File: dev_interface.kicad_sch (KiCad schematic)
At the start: 18 parts, among them U10 ADS1014IDGS, U11 DACx53401, U12 ADS1014IDGS, U4 TLV9302xD, U9 ISO164xB

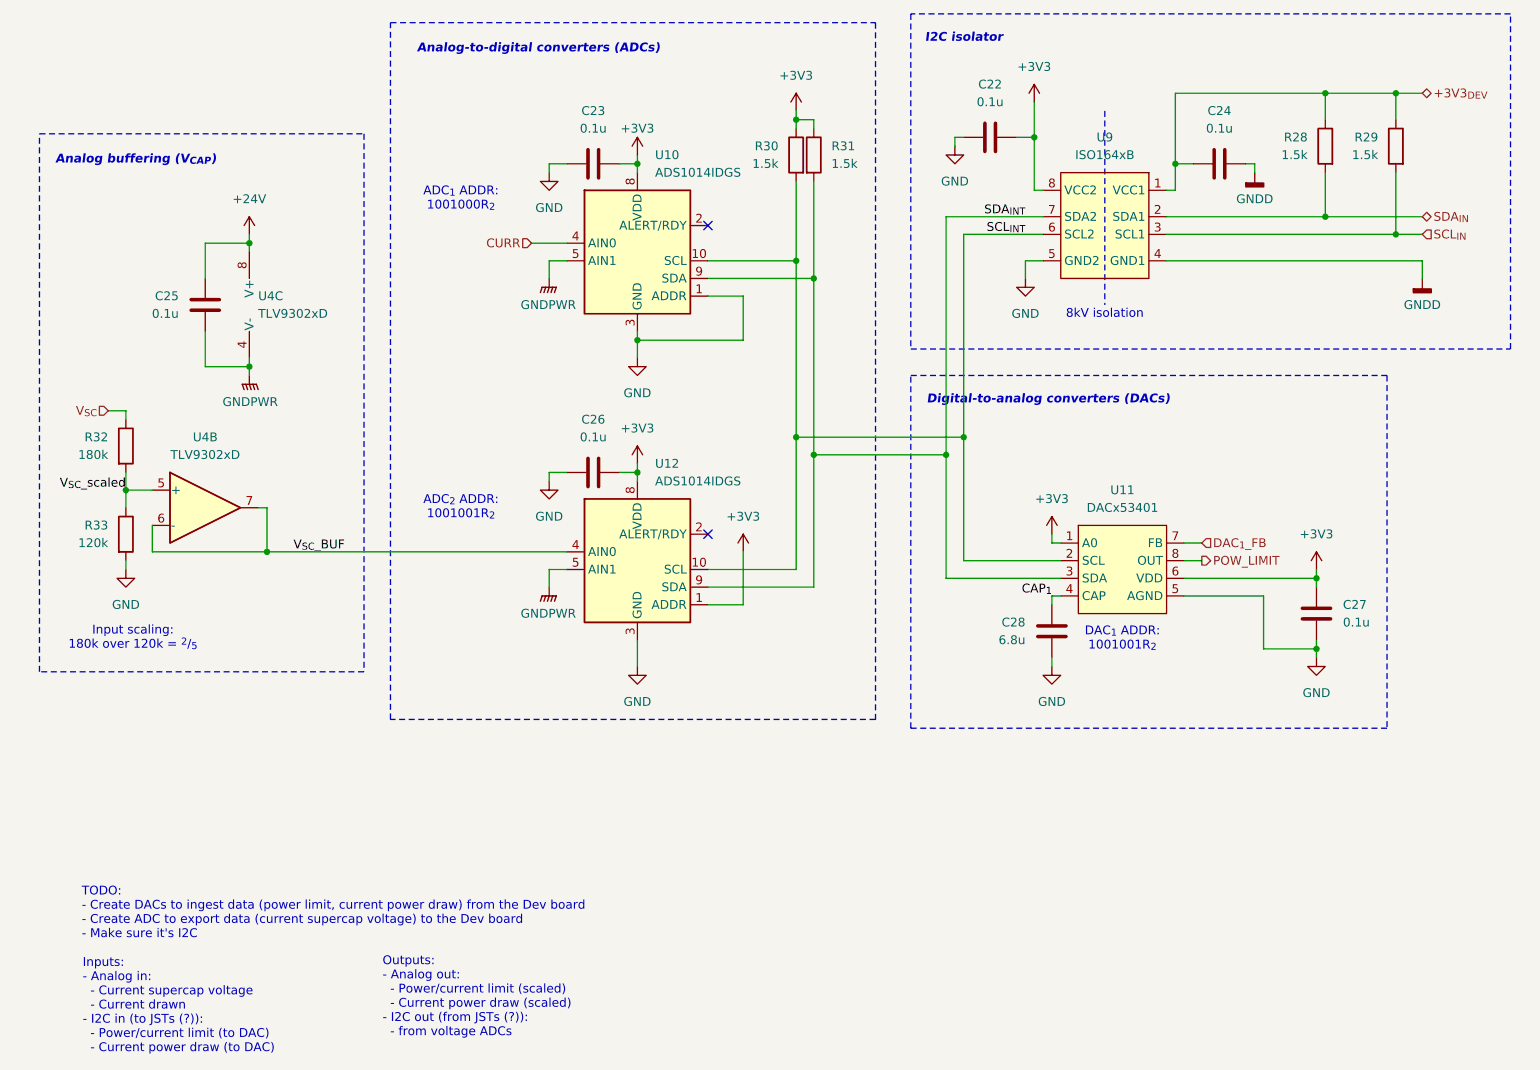
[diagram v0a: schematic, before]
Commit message: Correct symbol library path, renumber components
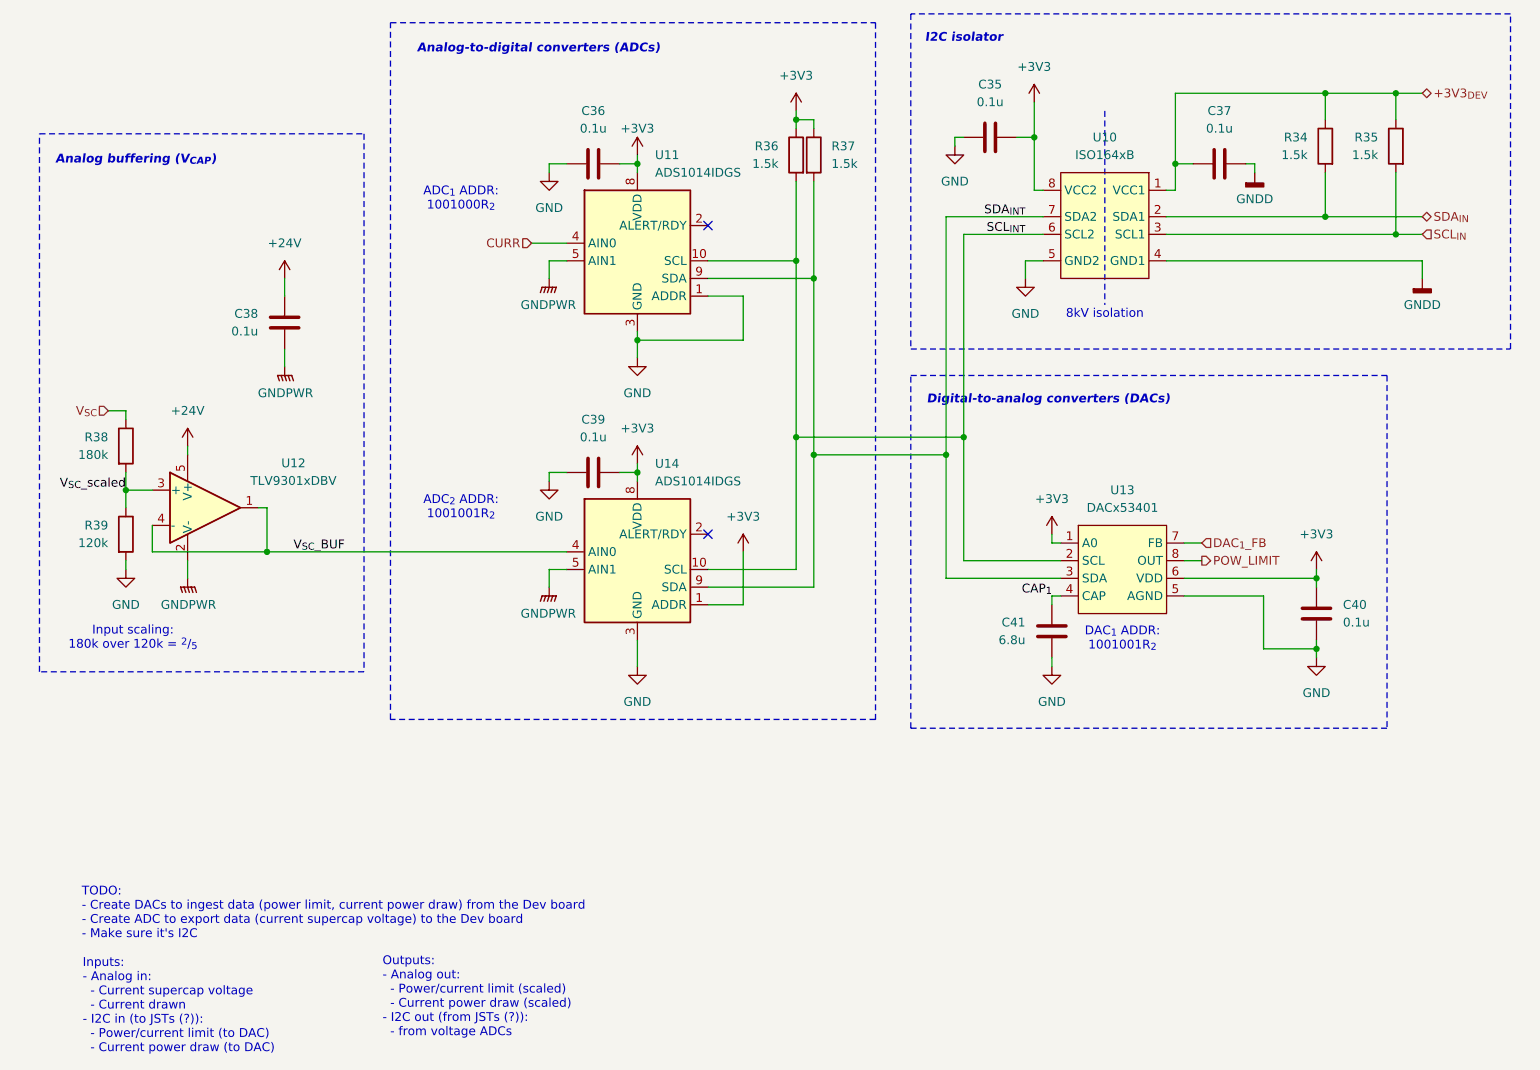
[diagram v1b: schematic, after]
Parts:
- removed U4: TLV9302xD, Package_SO:SOIC-8_3.9x4.9mm_P1.27mm, symbol Amplifier_Operational:TLV9302xD
- added U12: TLV9301xDBV, Package_TO_SOT_SMD:SOT-23-5_HandSoldering, symbol Amplifier_Operational:TLV9301xDBV
- renumbered C22 to C35, C23 to C36, C24 to C37, C25 to C38, C26 to C39, C27 to C40, C28 to C41, R28 to R34, R29 to R35, R30 to R36, R31 to R37, R32 to R38, R33 to R39, U9 to U10, U10 to U11, U11 to U13, U12 to U14
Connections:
- net +24V: now also U12.5 (V+)
- net GNDPWR: now also U12.2 (V-)
- net V_{SC}_BUF: now also U12.1, U12.4 (-)
- net V_{SC}_scaled: now also U12.3 (+)
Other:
- moved on the sheet: C38

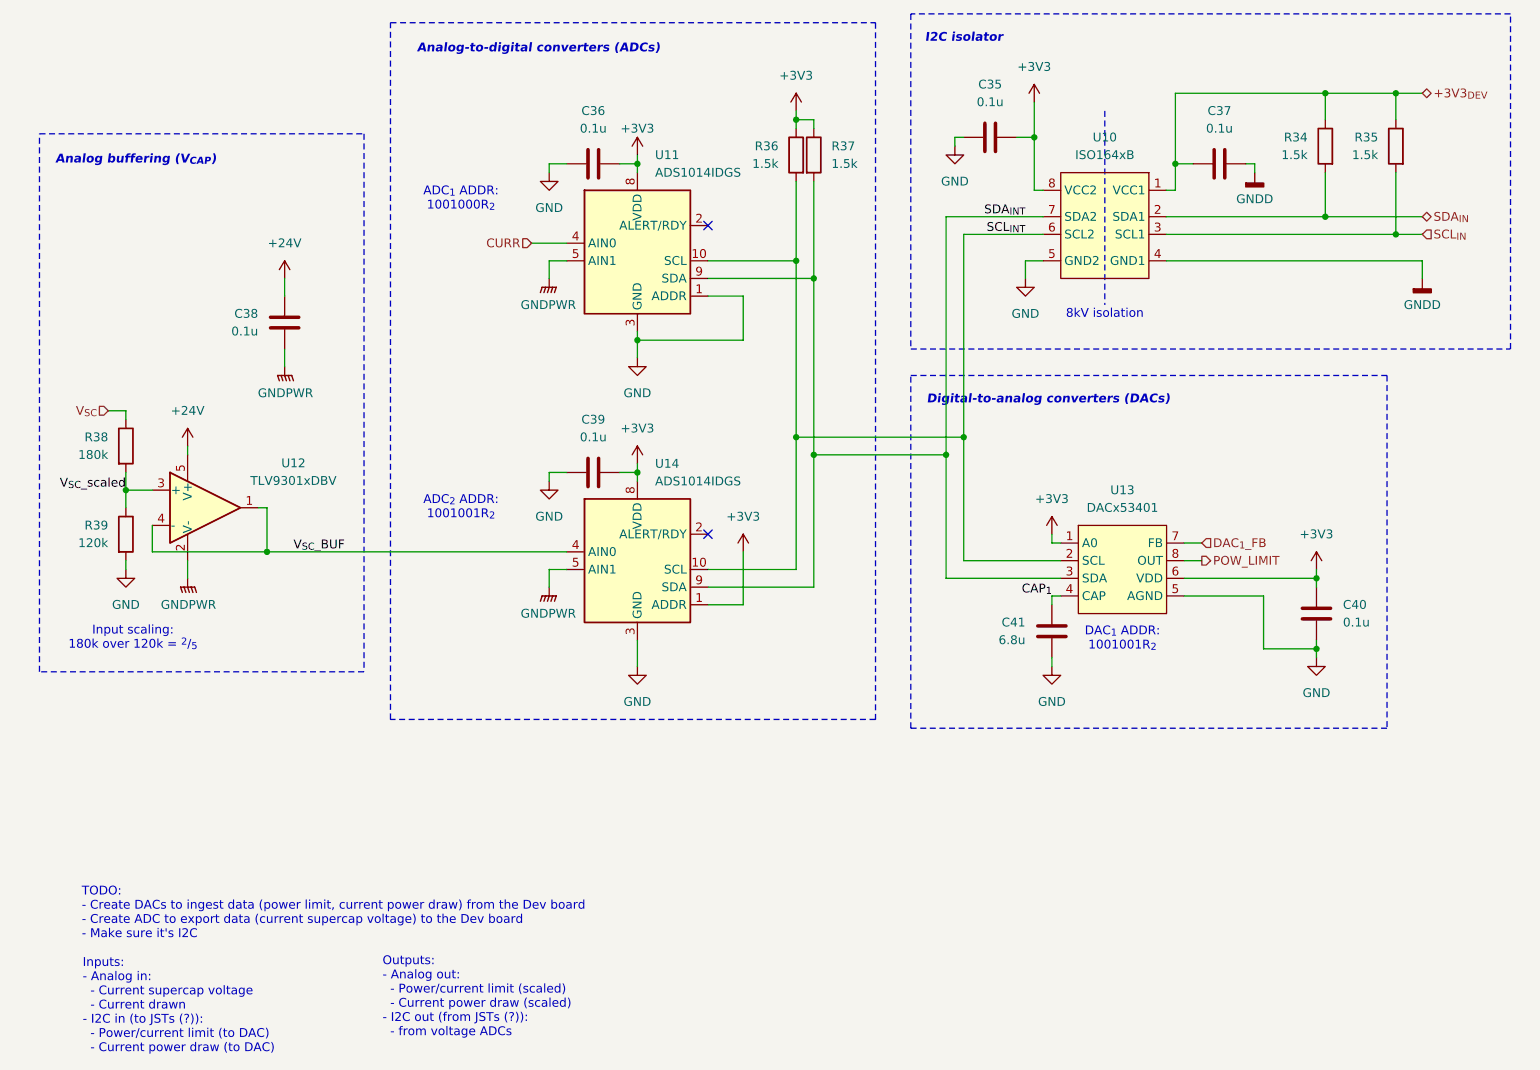
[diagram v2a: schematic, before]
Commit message: implemented dev board interface review suggestions as per morris
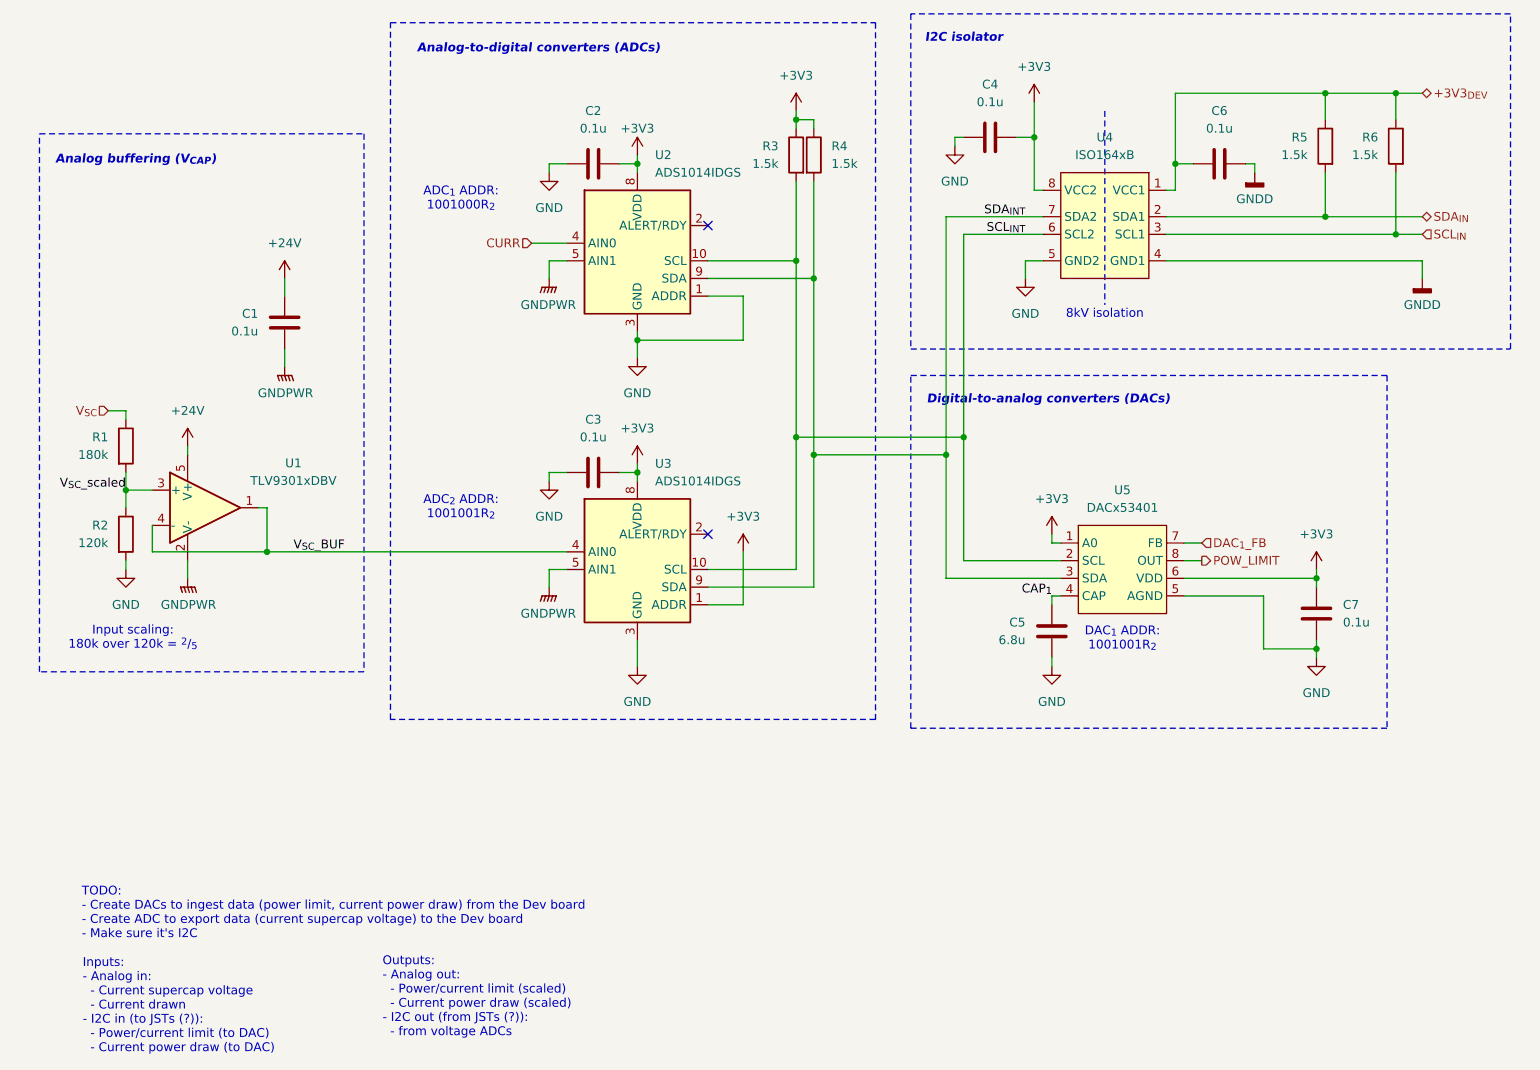
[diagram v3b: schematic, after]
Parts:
- renumbered C38 to C1, C36 to C2, C39 to C3, C35 to C4, C41 to C5, C37 to C6, C40 to C7, R38 to R1, R39 to R2, R36 to R3, R37 to R4, R34 to R5, R35 to R6, U12 to U1, U11 to U2, U14 to U3, U10 to U4, U13 to U5
